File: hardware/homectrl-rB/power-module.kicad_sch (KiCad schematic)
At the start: 0 parts

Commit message: power circuitry
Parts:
- added C1: 100uF 24V, symbol Device:C_Polarized
- added C2: 10uF 24V, symbol Device:C
- added C3, C5: 0.1uF 16V, symbol Device:C
- added C4: 3.3pF 16V, symbol Device:C
- added C6: 47uF 16V, symbol Device:C
- added C7: 0.47uF 12V, symbol Device:C
- added C8: 47uF 12V, symbol Device:C
- added D1: SS14, Diode_SMD:D_SMA, symbol Diode:SS14
- added D2: SMAJ15A, Diode_SMD:D_SMA, symbol Diode:SMAJ15A
- added D3: D_Zener, Diode_SMD:D_SOD-123F, symbol Device:D_Zener
- added D4, D5: LED, symbol Device:LED
- added D6: BUCK-LED, symbol Device:LED
- added F1: Polyfuse, symbol Device:Polyfuse
- added J1: Barrel_Jack, symbol Connector:Barrel_Jack
- added L1: L, symbol Device:L
- added Q1: FQP7P06, Package_TO_SOT_THT:TO-220-3_Vertical, symbol Transistor_FET:FQP27P06
- added R1: 15k, symbol Device:R
- added R2, R3: 100k, symbol Device:R
- added R4, R5: 4.7K, symbol Device:R
- added R6: 450, symbol Device:R
- added U2: TPS5405DR, TPS5405DR:SOIC127P599X175-8N, symbol TPS5405DR:TPS5405DR
- added VR1: LM3940IMP-3.3_NOPB, LM3940IMP-3.3_NOPB:VREG_LM3940IMP-3.3_NOPB, symbol LM3940IMP-3.3_NOPB:LM3940IMP-3.3_NOPB
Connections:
- new net: D6.2 (A), R4.1
- new net: D2.1 (A1), F1.2, Q1.2 (D), R4.2
- new net: F1.1, J1.1
- new net: C5.2, U2.4 (SS)
- new net: C3.1, D1.1 (K), L1.1, U2.8 (LX)
- new net: C4.1, R1.2
- new net: R3.2, U2.3 (ROSC)
- new net: C3.2, U2.1 (BOOT)
- new net: R1.1, U2.6 (COMP)
- new net: D3.2 (A), Q1.1 (G), R2.1
- new net: D5.2 (A), R6.2
- new net: D4.2 (A), R5.2
- new net +12V: C1.1, C2.2, D3.1 (K), Q1.3 (S), R5.1, U2.2 (VIN)
- new net +3V3: C8.2, R6.1, VR1.3 (OUT)
- new net +5V: C6.1, C7.2, L1.2, U2.5 (VSENSE), VR1.1 (IN)
- new net GND: C1.2, C2.1, C4.2, C5.1, C6.2, C7.1, C8.1, D1.2 (A), D2.2 (A2), D4.1 (K), D5.1 (K), D6.1 (K), J1.2, R2.2, R3.1, U2.7 (GND), VR1.2 (GND_2), VR1.4 (GND_4)
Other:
- note added: "P-IN"
- note added: "P-INDC"
- note added: "P-REG"
- note added: "V-OUT"

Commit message: assign footprints
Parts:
- added C10: 10uF 47uF, Capacitor_SMD:C_0603_1608Metric, symbol Device:C
- added C9: 47uF 12V, Diode_SMD:D_0805_2012Metric, symbol Device:C_Polarized
- C1: footprint (none) -> Capacitor_SMD:CP_Elec_6.3x5.8
- C2: footprint (none) -> Capacitor_SMD:C_0805_2012Metric
- C3, C5, C6, C7: footprint (none) -> Capacitor_SMD:C_0603_1608Metric
- C4: footprint (none) -> Capacitor_SMD:C_0402_1005Metric
- C8: footprint (none) -> Diode_SMD:D_0805_2012Metric
- D4: value LED -> 12V-LED; footprint (none) -> LED_SMD:LED_0805_2012Metric
- D5: value LED -> 3V3-LED; footprint (none) -> LED_SMD:LED_0805_2012Metric
- D6: footprint (none) -> LED_SMD:LED_0603_1608Metric
- F1: footprint (none) -> 1210L110_16WR:FUSC3226X125N
- J1: footprint (none) -> Connector_BarrelJack:BarrelJack_Horizontal
- L1: footprint (none) -> Inductor_SMD:L_Taiyo-Yuden_MD-5050
- R1, R2, R3, R6: footprint (none) -> Resistor_SMD:R_0402_1005Metric
- R4, R5: footprint (none) -> Resistor_SMD:R_0201_0603Metric
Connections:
- net +5V: now also C10.2, C9.1
- net GND: now also C10.1, C9.2
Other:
- moved on the sheet: C7

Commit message: pmux & breakout circuitry
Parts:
- added C11, C12: 1uF 12V, Capacitor_SMD:C_0805_2012Metric, symbol Device:C
- added TP4: TP_12V, TestPoint:TestPoint_Pad_1.0x1.0mm, symbol Connector:TestPoint
- added TP5: TP_3V3, TestPoint:TestPoint_Pad_1.0x1.0mm, symbol Connector:TestPoint
- added TP6: TP_12V-B, TestPoint:TestPoint_Pad_1.0x1.0mm, symbol Connector:TestPoint
- added U3, U4: ID_LM66100DCKR, LM66100:SC-70-6, symbol QRET_Buck_PSU:LM66100DCKR
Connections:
- net +12V: now also TP4.1
- net +3V3: now also TP5.1
- net +5V: now also U3.3 (*CE), U3.6 (VOUT), U4.3 (*CE), U4.6 (VOUT); no longer C6.1, L1.2, U2.5 (VSENSE)
- net GND: now also C11.2, C12.2, U3.2 (GND), U3.5 (ST), U4.2 (GND), U4.5 (ST)
- net at D2.1 (A1), F1.2, Q1.2 (D)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: now also TP6.1
- new net 5V-B: C11.1, C6.1, L1.2, U2.5 (VSENSE), U3.1 (VIN)
- new net 5V-U: C12.1, U4.1 (VIN)
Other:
- note added: "-> LDO"
- note added: "P-MUX"
- moved on the sheet: C1, C10, C2, C3, C4, C5, C6, C7, C8, C9, D1, D2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

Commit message: layout work
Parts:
- C5: value 0.1uF 16V -> 47nF 12V
- C8, C9: footprint Diode_SMD:D_0805_2012Metric -> Capacitor_SMD:C_0603_1608Metric
- L1: footprint Inductor_SMD:L_Taiyo-Yuden_MD-5050 -> VLS3015CX-220M-1:IND_VLS3015CX-220M-1
- Q1: value FQP7P06 -> DMP6023LE-13; footprint Package_TO_SOT_THT:TO-220-3_Vertical -> Package_TO_SOT_SMD:SOT-223
- R4, R5: footprint Resistor_SMD:R_0201_0603Metric -> Resistor_SMD:R_0603_1608Metric
- TP6: value TP_12V-B -> TP-5V-B
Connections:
- net 5V-B: now also TP6.1
- net at D2.1 (A1), F1.2, Q1.2 (D)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: no longer TP6.1
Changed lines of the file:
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@@
 	)
 	(junction
+		(at 113.03 111.76)
+		(diameter 0)
+		(color 0 0 0 0)
+	)
+	(junction
 		(at 161.29 105.41)
 		(diameter 0)
@@
 	)
 	(junction
-		(at 62.23 52.07)
-		(diameter 0)
-		(color 0 0 0 0)
-	)
-	(junction
 		(at 49.53 52.07)
 		(diameter 0)
@@
 	(wire
 		(pts
-			(xy 58.42 52.07) (xy 62.23 52.07)
-		)
-		(stroke
-			(width 0)
-			(type default)
-			(color 194 0 0 1)
-		)
-	)
-	(wire
-		(pts
-			(xy 62.23 52.07) (xy 64.77 52.07)
+			(xy 58.42 52.07) (xy 64.77 52.07)
 		)
 		(stroke
@@
 	(wire
 		(pts
+			(xy 113.03 111.76) (xy 115.57 111.76)
+		)
+		(stroke
+			(width 0)
+			(type default)
+		)
+	)
+	(wire
+		(pts
 			(xy 205.74 46.99) (xy 200.66 46.99)
 		)
@@
 	(wire
 		(pts
-			(xy 107.95 111.76) (xy 115.57 111.76)
+			(xy 107.95 111.76) (xy 113.03 111.76)
 		)
 		(stroke
@@
 	)
 	(symbol
-		(lib_id "Connector:TestPoint")
-		(at 62.23 52.07 0)
-		(unit 1)
-		(exclude_from_sim no)
-		(in_bom yes)
-		(on_board yes)
-		(dnp no)
-		(property "Reference" "TP6"
-			(at 62.23 40.64 0)
-			(effects
-				(font
-					(size 1.27 1.27)
-				)
-				(justify left)
-			)
-		)
-		(property "Value" "TP_12V-B"
-			(at 62.23 42.4181 0)
-			(effects
-				(font
-					(size 1.27 1.27)
-				)
-				(justify left)
-			)
-		)
-		(property "Footprint" "TestPoint:TestPoint_Pad_1.0x1.0mm"
-			(at 67.31 52.07 0)
-			(effects
-				(font
-					(size 1.27 1.27)
-				)
-				(hide yes)
-			)
-		)
-		(property "Datasheet" "~"
-			(at 67.31 52.07 0)
-			(effects
-				(font
-					(size 1.27 1.27)
-				)
-				(hide yes)
-			)
-		)
-		(property "Description" "test point"
-			(at 62.23 52.07 0)
-			(effects
-				(font
-					(size 1.27 1.27)
-				)
-				(hide yes)
-			)
-		)
-		(pin "1"
-		)
-		(instances
-			(project "homectrl-rB"
-				(path "/57d8224d-b57c-478b-b5c0-8f7e53702df5/c83a7989-d1c5-453e-9ef8-069559a5a4f1"
-					(reference "TP6")
-					(unit 1)
-				)
-			)
-		)
-	)
-	(symbol
 		(lib_id "Device:C")
 		(at 161.29 99.06 0)
@@
 			)
 		)
-		(property "Footprint" "Diode_SMD:D_0805_2012Metric"
+		(property "Footprint" "Capacitor_SMD:C_0603_1608Metric"
 			(at 162.2552 102.87 0)
 			(effects
@@
 			)
 		)
-		(property "Footprint" "Resistor_SMD:R_0201_0603Metric"
+		(property "Footprint" "Resistor_SMD:R_0603_1608Metric"
 			(at 56.642 48.26 90)
 			(effects
@@
 			)
 		)
-		(property "Value" "0.1uF 16V"
+		(property "Value" "47nF 12V"
 			(at 28.448 102.108 0)
 			(effects
@@
 			)
 		)
-		(property "Footprint" "Diode_SMD:D_0805_2012Metric"
+		(property "Footprint" "Capacitor_SMD:C_0603_1608Metric"
 			(at 268.9352 62.23 0)
 			(effects
@@
 			)
 		)
-		(property "Footprint" "Inductor_SMD:L_Taiyo-Yuden_MD-5050"
+		(property "Footprint" "VLS3015CX-220M-1:IND_VLS3015CX-220M-1"
 			(at 73.66 135.89 0)
 			(effects
@@
 			)
 		)
-		(property "Datasheet" "~"
+		(property "Datasheet" "https://product.tdk.com/en/system/files/dam/doc/product/inductor/inductor/smd/catalog/inductor_commercial_power_vls3015cx-1_en.pdf"
 			(at 73.66 135.89 0)
 			(effects
@@
 	)
 	(symbol
+		(lib_id "Connector:TestPoint")
+		(at 113.03 111.76 0)
+		(unit 1)
+		(exclude_from_sim no)
+		(in_bom yes)
+		(on_board yes)
+		(dnp no)
+		(property "Reference" "TP6"
+			(at 114.3 108.458 0)
+			(effects
+				(font
+					(size 1.27 1.27)
+				)
+				(justify left)
+			)
+		)
+		(property "Value" "TP-5V-B"
+			(at 118.11 113.538 0)
+			(effects
+				(font
+					(size 1.27 1.27)
+				)
+				(justify left)
+			)
+		)
+		(property "Footprint" "TestPoint:TestPoint_Pad_1.0x1.0mm"
+			(at 118.11 111.76 0)
+			(effects
+				(font
+					(size 1.27 1.27)
+				)
+				(hide yes)
+			)
+		)
+		(property "Datasheet" "~"
+			(at 118.11 111.76 0)
+			(effects
+				(font
+					(size 1.27 1.27)
+				)
+				(hide yes)
+			)
+		)
+		(property "Description" "test point"
+			(at 113.03 111.76 0)
+			(effects
+				(font
+					(size 1.27 1.27)
+				)
+				(hide yes)
+			)
+		)
+		(pin "1"
+		)
+		(instances
+			(project ""
+				(path "/57d8224d-b57c-478b-b5c0-8f7e53702df5/c83a7989-d1c5-453e-9ef8-069559a5a4f1"
+					(reference "TP6")
+					(unit 1)
+				)
+			)
+		)
+	)
+	(symbol
 		(lib_id "power:PWR_FLAG")
 		(at 107.95 111.76 180)
@@
 		(on_board yes)
 		(dnp no)
-		(fields_autoplaced yes)
 		(property "Reference" "Q1"
-			(at 69.85 45.72 90)
+			(at 72.39 45.466 90)
 			(effects
 				(font
@@
 			)
 		)
-		(property "Value" "FQP7P06"
-			(at 69.85 48.26 90)
+		(property "Value" "DMP6023LE-13"
+			(at 72.39 48.006 90)
 			(effects
 				(font
@@
 			)
 		)
-		(property "Footprint" "Package_TO_SOT_THT:TO-220-3_Vertical"
+		(property "Footprint" "Package_TO_SOT_SMD:SOT-223"
 			(at 71.755 49.53 0)
 			(effects
@@
 			)
 		)
-		(property "Footprint" "Resistor_SMD:R_0201_0603Metric"
+		(property "Footprint" "Resistor_SMD:R_0603_1608Metric"
 			(at 150.622 49.53 90)
 			(effects

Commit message: W
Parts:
- C1, C10, C11, C12, C2, C3, C4, C5, C6, C7, C8, C9, D1, D2, D3, D4, D5, D6, F1, L1, Q1, R1, R2, R3, R4, R5, U2, U3, U4, VR1: Purchase (none) -> Yes
- J1: Purchase (none) -> No; now not fitted
- R6, TP4, TP5, TP6: Purchase (none) -> N/A

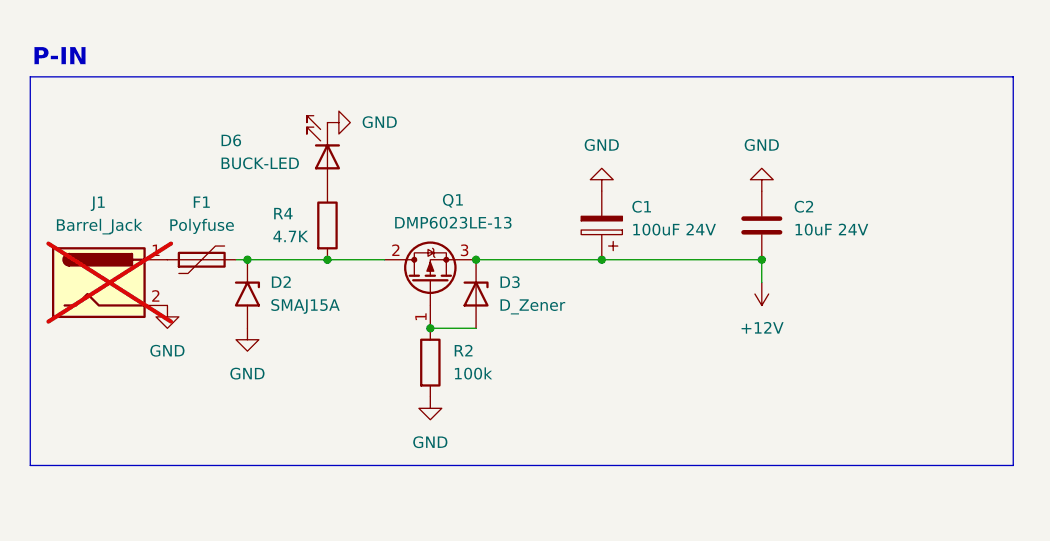
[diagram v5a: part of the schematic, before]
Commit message: add new caps, add ferrite bead, add MPNs
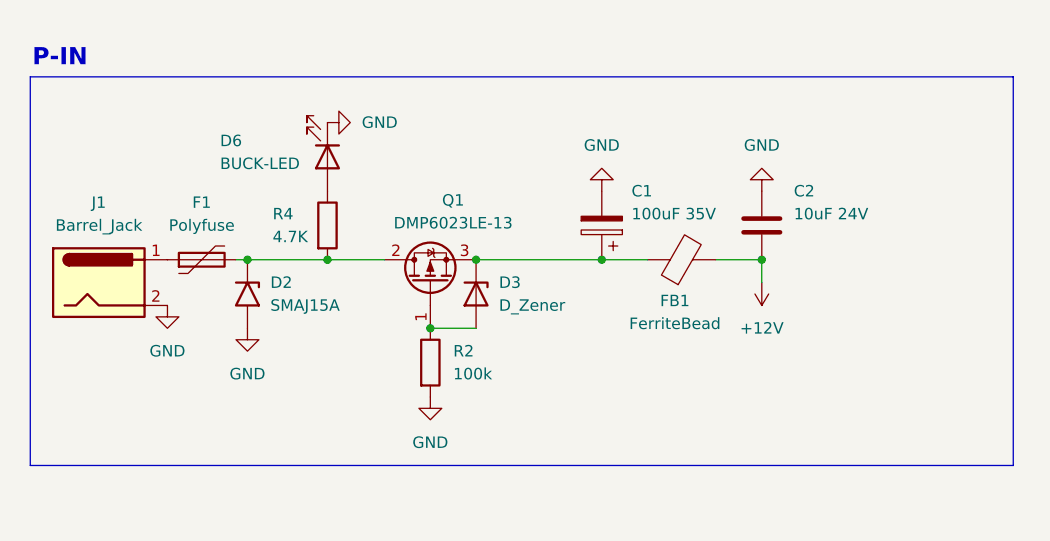
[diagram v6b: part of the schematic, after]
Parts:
- added FB1: FerriteBead, MPZ2012S221AT000:BEADC2012X105N, symbol Device:FerriteBead
- C1: value 100uF 24V -> 100uF 35V; footprint Capacitor_SMD:CP_Elec_6.3x5.8 -> EEE_FK1V101P:CAP_EEEFK1V101P; MPN (none) -> EEE-FK1V101P
- D1: MPN (none) -> SS14
- D2: MPN (none) -> SMAJ15A
- F1: MPN (none) -> 1210L110/16WR
- J1: MPN (none) -> N/A; now fitted
- Q1: MPN (none) -> DMP6023LE-13
- R6: Purchase N/A -> Yes
- TP4, TP5, TP6: MPN (none) -> N/A
- U2: MPN (none) -> TPS5405DR
- U3, U4: MPN (none) -> LM66100DCKR
- VR1: MPN (none) -> LM3940IMP-3.3/NOPB
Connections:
- net +12V: now also FB1.2; no longer C1.1, D3.1 (K), Q1.3 (S)
- new net: C1.1, D3.1 (K), FB1.1, Q1.3 (S)
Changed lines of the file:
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@@
 	(wire
 		(pts
+			(xy 101.6 52.07) (xy 106.68 52.07)
+		)
+		(stroke
+			(width 0)
+			(type default)
+			(color 194 0 0 1)
+		)
+	)
+	(wire
+		(pts
 			(xy 58.42 52.07) (xy 64.77 52.07)
 		)
@@
 	(wire
 		(pts
-			(xy 88.9 52.07) (xy 106.68 52.07)
+			(xy 88.9 52.07) (xy 93.98 52.07)
 		)
 		(stroke
@@
 			)
 		)
-		(property "MPN" ""
+		(property "MPN" "N/A"
 			(at 148.59 45.72 0)
 			(effects
@@
 			)
 		)
-		(property "MPN" ""
+		(property "MPN" "LM3940IMP-3.3/NOPB"
 			(at 143.51 107.95 0)
 			(effects
@@
 			)
 		)
-		(property "MPN" ""
+		(property "MPN" "SMAJ15A"
 			(at 49.53 55.88 0)
 			(effects
@@
 		(in_bom yes)
 		(on_board yes)
-		(dnp yes)
+		(dnp no)
 		(property "Reference" "J1"
 			(at 33.02 45.72 0)
@@
 			)
 		)
-		(property "MPN" ""
+		(property "MPN" "N/A"
 			(at 33.02 54.61 0)
 			(effects
@@
 			)
 		)
-		(property "MPN" ""
+		(property "MPN" "SS14"
 			(at 64.77 139.7 0)
 			(effects
@@
 			)
 		)
-		(property "MPN" ""
+		(property "MPN" "LM66100DCKR"
 			(at 233.68 60.96 0)
 			(effects
@@
 			)
 		)
-		(property "MPN" ""
+		(property "MPN" "TPS5405DR"
 			(at 72.39 115.57 0)
 			(effects
@@
 			)
 		)
-		(property "MPN" ""
+		(property "MPN" "LM66100DCKR"
 			(at 233.68 41.91 0)
 			(effects
@@
 		(dnp no)
 		(property "Reference" "C2"
-			(at 110.236 46.228 0)
+			(at 110.236 44.45 0)
 			(effects
 				(font
@@
 		)
 		(property "Value" "10uF 24V"
-			(at 110.236 48.768 0)
+			(at 110.236 46.99 0)
 			(effects
 				(font
@@
 	)
 	(symbol
+		(lib_id "Device:FerriteBead")
+		(at 97.79 52.07 90)
+		(unit 1)
+		(exclude_from_sim no)
+		(in_bom yes)
+		(on_board yes)
+		(dnp no)
+		(property "Reference" "FB1"
+			(at 97.028 56.642 90)
+			(effects
+				(font
+					(size 1.27 1.27)
+				)
+			)
+		)
+		(property "Value" "FerriteBead"
+			(at 97.028 59.182 90)
+			(effects
+				(font
+					(size 1.27 1.27)
+				)
+			)
+		)
+		(property "Footprint" "MPZ2012S221AT000:BEADC2012X105N"
+			(at 97.79 53.848 90)
+			(effects
+				(font
+					(size 1.27 1.27)
+				)
+				(hide yes)
+			)
+		)
+		(property "Datasheet" "https://product.tdk.com/system/files/dam/doc/product/emc/emc/beads/catalog/beads_commercial_power_mpz2012_en.pdf"
+			(at 97.79 52.07 0)
+			(effects
+				(font
+					(size 1.27 1.27)
+				)
+				(hide yes)
+			)
+		)
+		(property "Description" "Ferrite bead"
+			(at 97.79 52.07 0)
+			(effects
+				(font
+					(size 1.27 1.27)
+				)
+				(hide yes)
+			)
+		)
+		(property "MPN" "MPZ2012S221AT000"
+			(at 97.79 52.07 0)
+			(effects
+				(font
+					(size 1.27 1.27)
+				)
+				(hide yes)
+			)
+		)
+		(pin "1"
+		)
+		(pin "2"
+		)
+		(instances
+			(project ""
+				(path "/57d8224d-b57c-478b-b5c0-8f7e53702df5/c83a7989-d1c5-453e-9ef8-069559a5a4f1"
+					(reference "FB1")
+					(unit 1)
+				)
+			)
+		)
+	)
+	(symbol
 		(lib_id "Device:LED")
 		(at 58.42 40.64 270)
@@
 			)
 		)
-		(property "MPN" ""
+		(property "MPN" "N/A"
 			(at 172.72 45.72 0)
 			(effects
@@
 			)
 		)
-		(property "Purchase" "N/A"
+		(property "Purchase" "Yes"
 			(at 167.64 49.53 0)
 			(effects
@@
 			)
 		)
-		(property "MPN" ""
+		(property "MPN" "N/A"
 			(at 113.03 111.76 0)
 			(effects
@@
 		(dnp no)
 		(property "Reference" "C1"
-			(at 92.202 46.228 0)
+			(at 92.202 44.45 0)
 			(effects
 				(font
@@
 			)
 		)
-		(property "Value" "100uF 24V"
-			(at 92.202 48.768 0)
+		(property "Value" "100uF 35V"
+			(at 92.202 46.99 0)
 			(effects
 				(font
@@
 			)
 		)
-		(property "Footprint" "Capacitor_SMD:CP_Elec_6.3x5.8"
+		(property "Footprint" "EEE_FK1V101P:CAP_EEEFK1V101P"
 			(at 87.9348 44.45 0)
 			(effects
@@
 			)
 		)
-		(property "MPN" ""
+		(property "MPN" "EEE-FK1V101P"
 			(at 88.9 48.26 0)
 			(effects
@@
 		(on_board yes)
 		(dnp no)
-		(fields_autoplaced yes)
 		(property "Reference" "F1"
 			(at 44.45 45.72 90)
@@
 			)
 		)
-		(property "MPN" ""
+		(property "MPN" "1210L110/16WR"
 			(at 44.45 52.07 0)
 			(effects
@@
 			)
 		)
-		(property "MPN" ""
+		(property "MPN" "DMP6023LE-13"
 			(at 69.85 54.61 0)
 			(effects
